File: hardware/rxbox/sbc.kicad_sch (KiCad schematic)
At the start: 0 parts

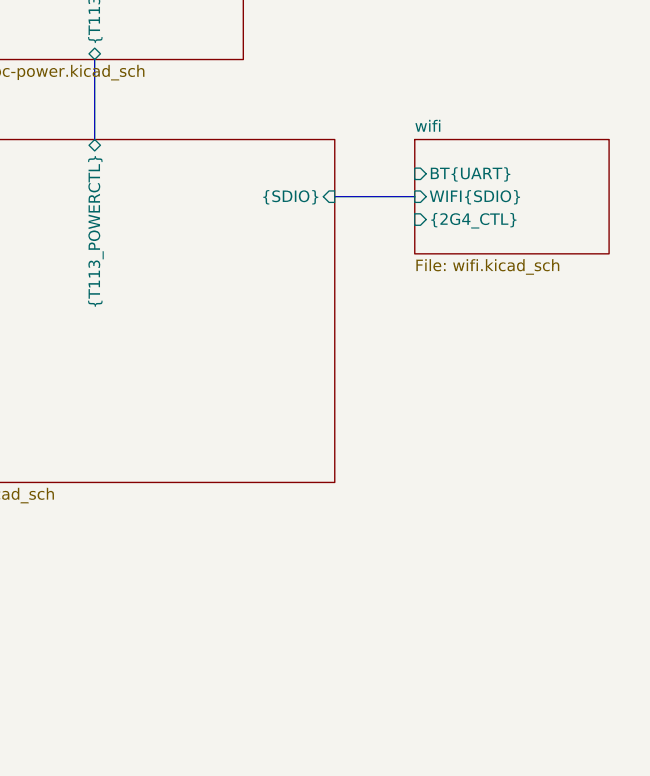
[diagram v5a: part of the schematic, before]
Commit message: finish hooking up wifi+bt, and power
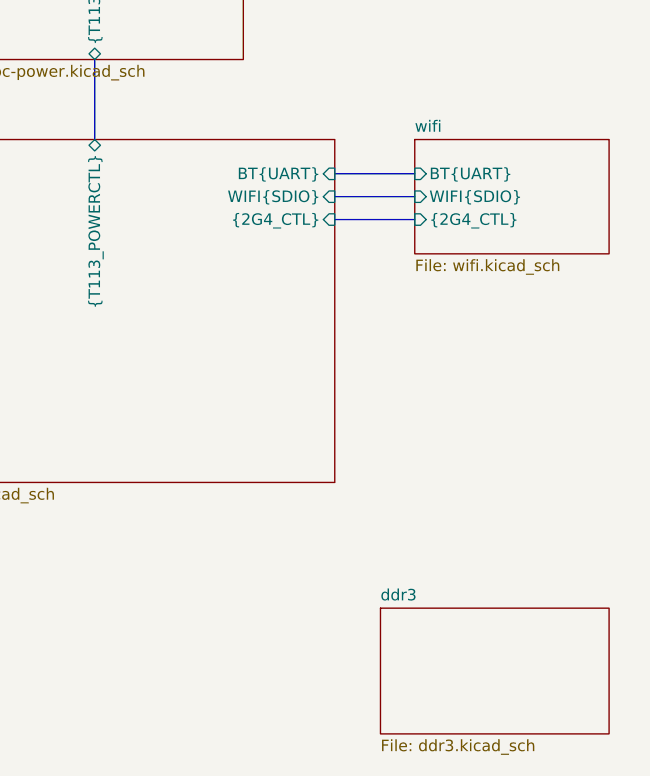
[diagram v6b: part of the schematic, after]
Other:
- added sheet ddr3 (ddr3.kicad_sch)
- sheet t113 ports: added BT{UART}, WIFI{SDIO}, {2G4_CTL}; removed {SDIO}
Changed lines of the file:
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@@
+	(bus
+		(pts
+			(xy 147.32 67.31) (xy 156.21 67.31)
+		)
+		(stroke
+			(width 0)
+			(type default)
+		)
+	)
+	(bus
+		(pts
+			(xy 147.32 72.39) (xy 156.21 72.39)
+		)
+		(stroke
+			(width 0)
+			(type default)
+		)
+	)
 	(bus
 		(pts
@@
 	)
 	(sheet
+		(at 152.4 115.57)
+		(size 25.4 13.97)
+		(exclude_from_sim no)
+		(in_bom yes)
+		(on_board yes)
+		(dnp no)
+		(fields_autoplaced yes)
+		(stroke
+			(width 0.1524)
+			(type solid)
+		)
+		(fill
+			(color 0 0 0 0)
+		)
+		(property "Sheetname" "ddr3"
+			(at 152.4 114.8584 0)
+			(show_name no)
+			(do_not_autoplace no)
+			(effects
+				(font
+					(size 1.27 1.27)
+				)
+				(justify left bottom)
+			)
+		)
+		(property "Sheetfile" "ddr3.kicad_sch"
+			(at 152.4 130.1246 0)
+			(show_name no)
+			(do_not_autoplace no)
+			(effects
+				(font
+					(size 1.27 1.27)
+				)
+				(justify left top)
+			)
+		)
+		(instances
+			(project "rxbox"
+				(path "/4bda69c0-d40e-4af8-940b-109cd2045912/e6dabd82-beec-4023-a66f-b67e0b07de29"
+					(page "8")
+				)
+			)
+		)
+	)
+	(sheet
 		(at 99.06 63.5)
 		(size 48.26 38.1)
@@
 			)
 		)
-		(pin "{SDIO}" input
+		(pin "BT{UART}" input
+			(at 147.32 67.31 0)
+			(effects
+				(font
+					(size 1.27 1.27)
+				)
+				(justify right)
+			)
+		)
+		(pin "WIFI{SDIO}" input
 			(at 147.32 69.85 0)
 			(effects
 				(font
+					(size 1.27 1.27)
+				)
+				(justify right)
+			)
+		)
+		(pin "{2G4_CTL}" input
+			(at 147.32 72.39 0)
+			(effects
+				(font

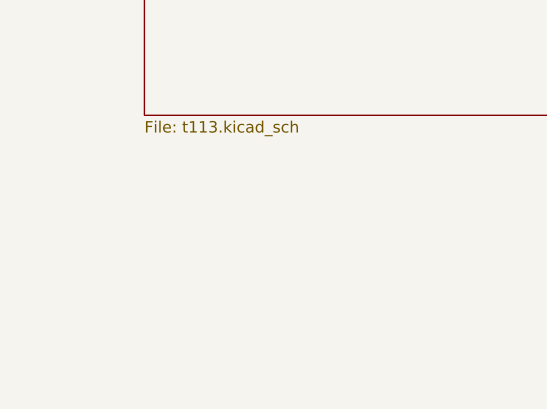
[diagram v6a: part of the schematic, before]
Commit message: start boot media circuitry
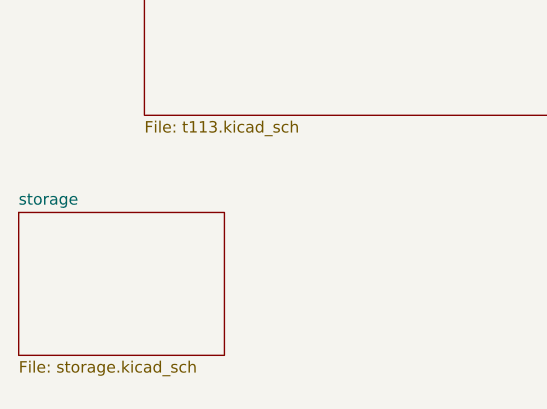
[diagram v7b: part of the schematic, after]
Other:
- added sheet storage (storage.kicad_sch)
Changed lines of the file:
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@@
+	)
+	(sheet
+		(at 85.09 112.395)
+		(size 22.86 15.875)
+		(exclude_from_sim no)
+		(in_bom yes)
+		(on_board yes)
+		(dnp no)
+		(fields_autoplaced yes)
+		(stroke
+			(width 0.1524)
+			(type solid)
+		)
+		(fill
+			(color 0 0 0 0)
+		)
+		(property "Sheetname" "storage"
+			(at 85.09 111.6834 0)
+			(show_name no)
+			(do_not_autoplace no)
+			(effects
+				(font
+					(size 1.27 1.27)
+				)
+				(justify left bottom)
+			)
+		)
+		(property "Sheetfile" "storage.kicad_sch"
+			(at 85.09 128.8546 0)
+			(show_name no)
+			(do_not_autoplace no)
+			(effects
+				(font
+					(size 1.27 1.27)
+				)
+				(justify left top)
+			)
+		)
+		(instances
+			(project "rxbox"
+				(path "/4bda69c0-d40e-4af8-940b-109cd2045912/e6dabd82-beec-4023-a66f-b67e0b07de29"
+					(page "9")
+				)
+			)
+		)
 	)
 	(sheet

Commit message: draft of ddr circuitry
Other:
- sheet ddr3 ports: added {DDR_ADDR}, {DDR_CLOCK}, {DDR_CMD}, {DDR_DATA}; removed none
- sheet storage ports: added NOR{SPI WP HOLD}, {SDHC}; removed none
- sheet t113 ports: added NOR{SPI WP HOLD}, SDBOOT{SDHC}, {DDR_ADDR}, {DDR_CLOCK}, {DDR_CMD}, {DDR_DATA}; removed none
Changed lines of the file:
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@@
+	(bus
+		(pts
+			(xy 114.3 101.6) (xy 114.3 107.95)
+		)
+		(stroke
+			(width 0)
+			(type default)
+		)
+	)
+	(bus
+		(pts
+			(xy 111.76 101.6) (xy 111.76 107.95)
+		)
+		(stroke
+			(width 0)
+			(type default)
+		)
+	)
 	(bus
 		(pts
@@
 		(pts
 			(xy 120.65 54.61) (xy 120.65 63.5)
+		)
+		(stroke
+			(width 0)
+			(type default)
+		)
+	)
+	(bus
+		(pts
+			(xy 134.62 101.6) (xy 134.62 107.95)
+		)
+		(stroke
+			(width 0)
+			(type default)
+		)
+	)
+	(bus
+		(pts
+			(xy 106.68 101.6) (xy 106.68 107.95)
+		)
+		(stroke
+			(width 0)
+			(type default)
+		)
+	)
+	(bus
+		(pts
+			(xy 137.16 101.6) (xy 137.16 107.95)
+		)
+		(stroke
+			(width 0)
+			(type default)
+		)
+	)
+	(bus
+		(pts
+			(xy 109.22 101.6) (xy 109.22 107.95)
 		)
 		(stroke
@@
 	)
 	(sheet
-		(at 85.09 112.395)
-		(size 22.86 15.875)
+		(at 125.73 107.95)
+		(size 20.32 25.4)
 		(exclude_from_sim no)
 		(in_bom yes)
@@
 		)
 		(property "Sheetname" "storage"
-			(at 85.09 111.6834 0)
+			(at 125.73 107.2384 0)
 			(show_name no)
 			(do_not_autoplace no)
@@
 		)
 		(property "Sheetfile" "storage.kicad_sch"
-			(at 85.09 128.8546 0)
+			(at 125.73 133.9346 0)
 			(show_name no)
 			(do_not_autoplace no)
@@
 				)
 				(justify left top)
+			)
+		)
+		(pin "NOR{SPI WP HOLD}" input
+			(at 137.16 107.95 90)
+			(effects
+				(font
+					(size 1.27 1.27)
+				)
+				(justify right)
+			)
+		)
+		(pin "{SDHC}" input
+			(at 134.62 107.95 90)
+			(effects
+				(font
+					(size 1.27 1.27)
+				)
+				(justify right)
 			)
 		)
@@
 	)
 	(sheet
-		(at 152.4 115.57)
-		(size 25.4 13.97)
+		(at 100.33 107.95)
+		(size 20.32 25.4)
 		(exclude_from_sim no)
 		(in_bom yes)
@@
 		)
 		(property "Sheetname" "ddr3"
-			(at 152.4 114.8584 0)
+			(at 100.33 107.2384 0)
 			(show_name no)
 			(do_not_autoplace no)
@@
 		)
 		(property "Sheetfile" "ddr3.kicad_sch"
-			(at 152.4 130.1246 0)
+			(at 100.33 133.9346 0)
 			(show_name no)
 			(do_not_autoplace no)
@@
 				)
 				(justify left top)
+			)
+		)
+		(pin "{DDR_DATA}" bidirectional
+			(at 109.22 107.95 90)
+			(effects
+				(font
+					(size 1.27 1.27)
+				)
+				(justify right)
+			)
+		)
+		(pin "{DDR_CLOCK}" input
+			(at 114.3 107.95 90)
+			(effects
+				(font
+					(size 1.27 1.27)
+				)
+				(justify right)
+			)
+		)
+		(pin "{DDR_ADDR}" bidirectional
+			(at 106.68 107.95 90)
+			(effects
+				(font
+					(size 1.27 1.27)
+				)
+				(justify right)
+			)
+		)
+		(pin "{DDR_CMD}" input
+			(at 111.76 107.95 90)
+			(effects
+				(font
+					(size 1.27 1.27)
+				)
+				(justify right)
 			)
 		)
@@
 			)
 		)
+		(pin "SDBOOT{SDHC}" input
+			(at 134.62 101.6 270)
+			(effects
+				(font
+					(size 1.27 1.27)
+				)
+				(justify left)
+			)
+		)
+		(pin "NOR{SPI WP HOLD}" input
+			(at 137.16 101.6 270)
+			(effects
+				(font
+					(size 1.27 1.27)
+				)
+				(justify left)
+			)
+		)
+		(pin "{DDR_CMD}" input
+			(at 111.76 101.6 270)
+			(effects
+				(font
+					(size 1.27 1.27)
+				)
+				(justify left)
+			)
+		)
+		(pin "{DDR_ADDR}" bidirectional
+			(at 106.68 101.6 270)
+			(effects
+				(font
+					(size 1.27 1.27)
+				)
+				(justify left)
+			)
+		)
+		(pin "{DDR_CLOCK}" input
+			(at 114.3 101.6 270)
+			(effects
+				(font
+					(size 1.27 1.27)
+				)
+				(justify left)
+			)
+		)
+		(pin "{DDR_DATA}" bidirectional
+			(at 109.22 101.6 270)
+			(effects
+				(font
+					(size 1.27 1.27)
+				)
+				(justify left)
+			)
+		)
